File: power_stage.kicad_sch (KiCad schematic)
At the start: 39 parts, among them IC2 L6498D, IC6 L6498D, IC7 L6498D, Q1 IPB320N20N3GATMA1, Q2 IPB320N20N3GATMA1, Q3 IPB320N20N3GATMA1, Q4 IPB320N20N3GATMA1, Q5 IPB320N20N3GATMA1, Q6 IPB320N20N3GATMA1

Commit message: Initial layout
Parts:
- added R24, R33, R34: 2.2Ω, Resistor_SMD:R_0603_1608Metric, symbol Device:R_Small_US
- C17, C18, C2, C20, C3, C8, Cboot1, Cboot2, Cboot3: footprint (none) -> Capacitor_SMD:C_0603_1608Metric
- R1, R10, R12, R13, R14, R15, R2, R3, R4, R7, R8, R9: footprint (none) -> Resistor_SMD:R_0603_1608Metric
- R11, R16, R5: footprint (none) -> Resistor_SMD:R_1206_3216Metric
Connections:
- net +12V: now also R24.2, R33.2, R34.2
- net at IC6.8 (BOOT): now also Cboot2.1, D2.1 (K); no longer D2.2 (A)
- net at Cboot1.1, D1.1 (K): now also IC2.8 (BOOT)
- net at D1.2 (A): now also R24.1; no longer IC2.8 (BOOT)
- net at IC7.8 (BOOT): now also Cboot3.1, D3.1 (K); no longer D3.2 (A)
- new net: D2.2 (A), R33.1
- new net: D3.2 (A), R34.1
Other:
- moved on the sheet: Cboot1, D1

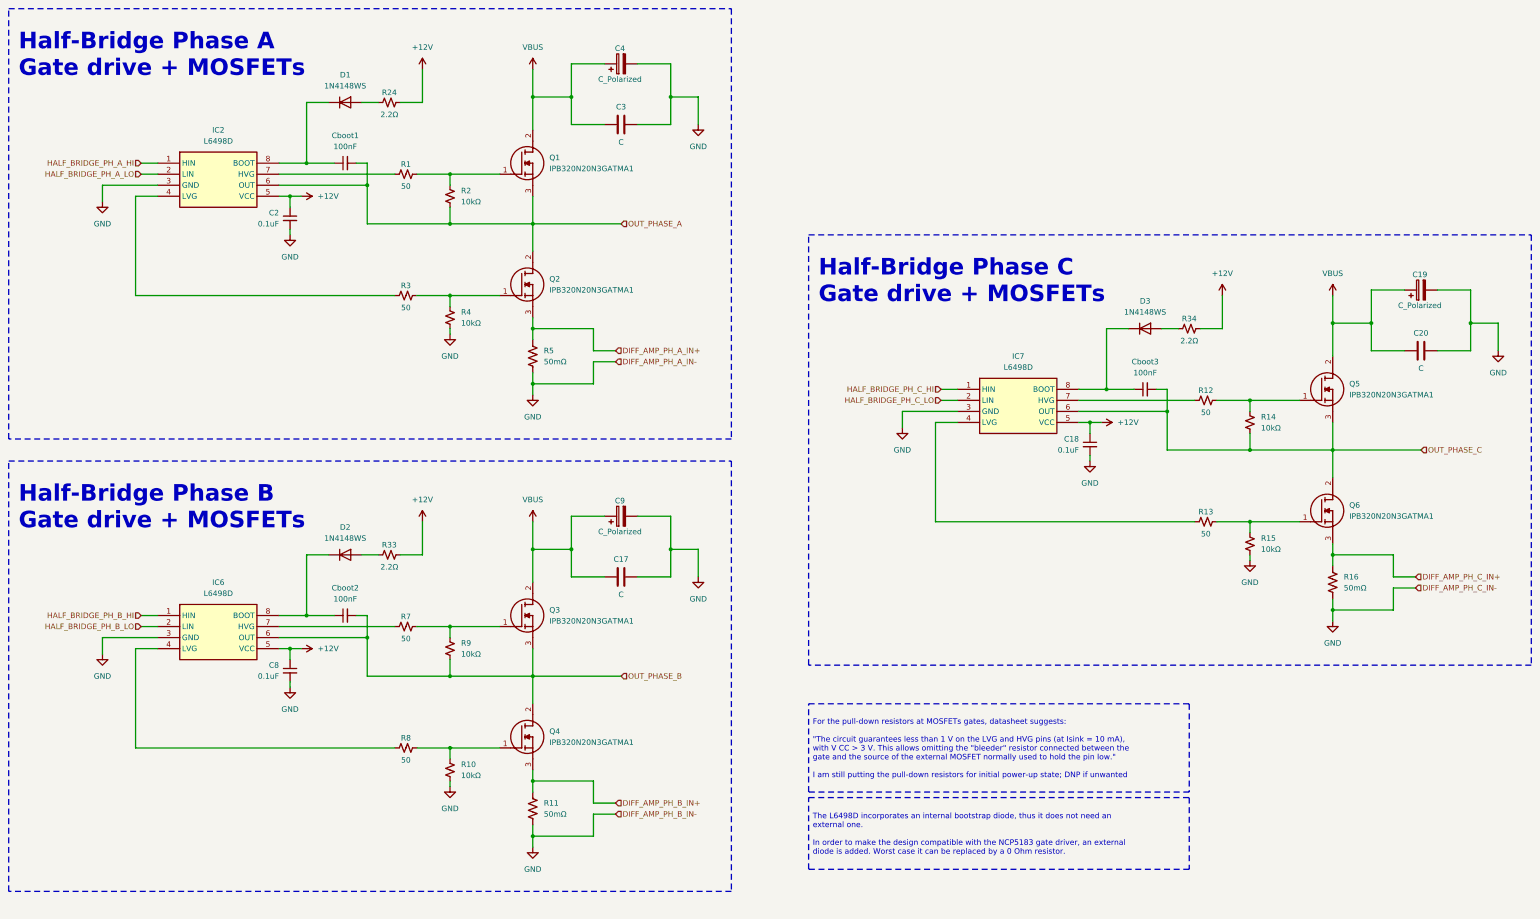
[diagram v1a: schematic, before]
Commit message: Almost all routing done
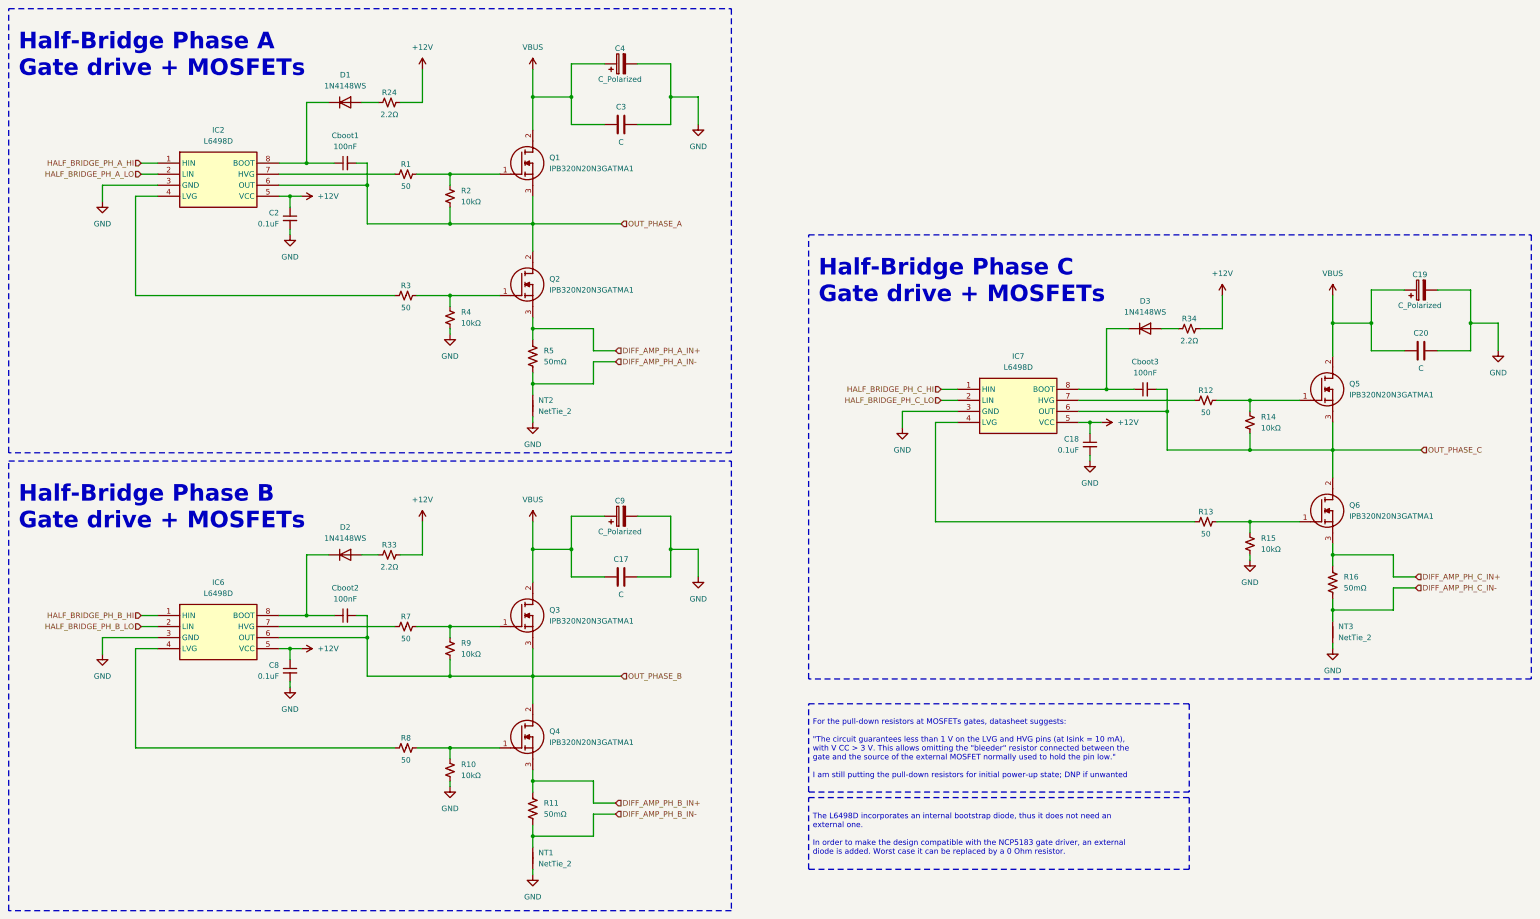
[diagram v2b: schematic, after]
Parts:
- added NT1, NT2, NT3: NetTie_2, NetTie:NetTie-2_SMD_Pad0.5mm, symbol Device:NetTie_2
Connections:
- net GND: now also NT1.1, NT2.1, NT3.1; no longer R11.2, R16.2, R5.2
- new net DIFF_AMP_PH_A_IN-: NT2.2, R5.2
- new net DIFF_AMP_PH_B_IN-: NT1.2, R11.2
- new net DIFF_AMP_PH_C_IN-: NT3.2, R16.2

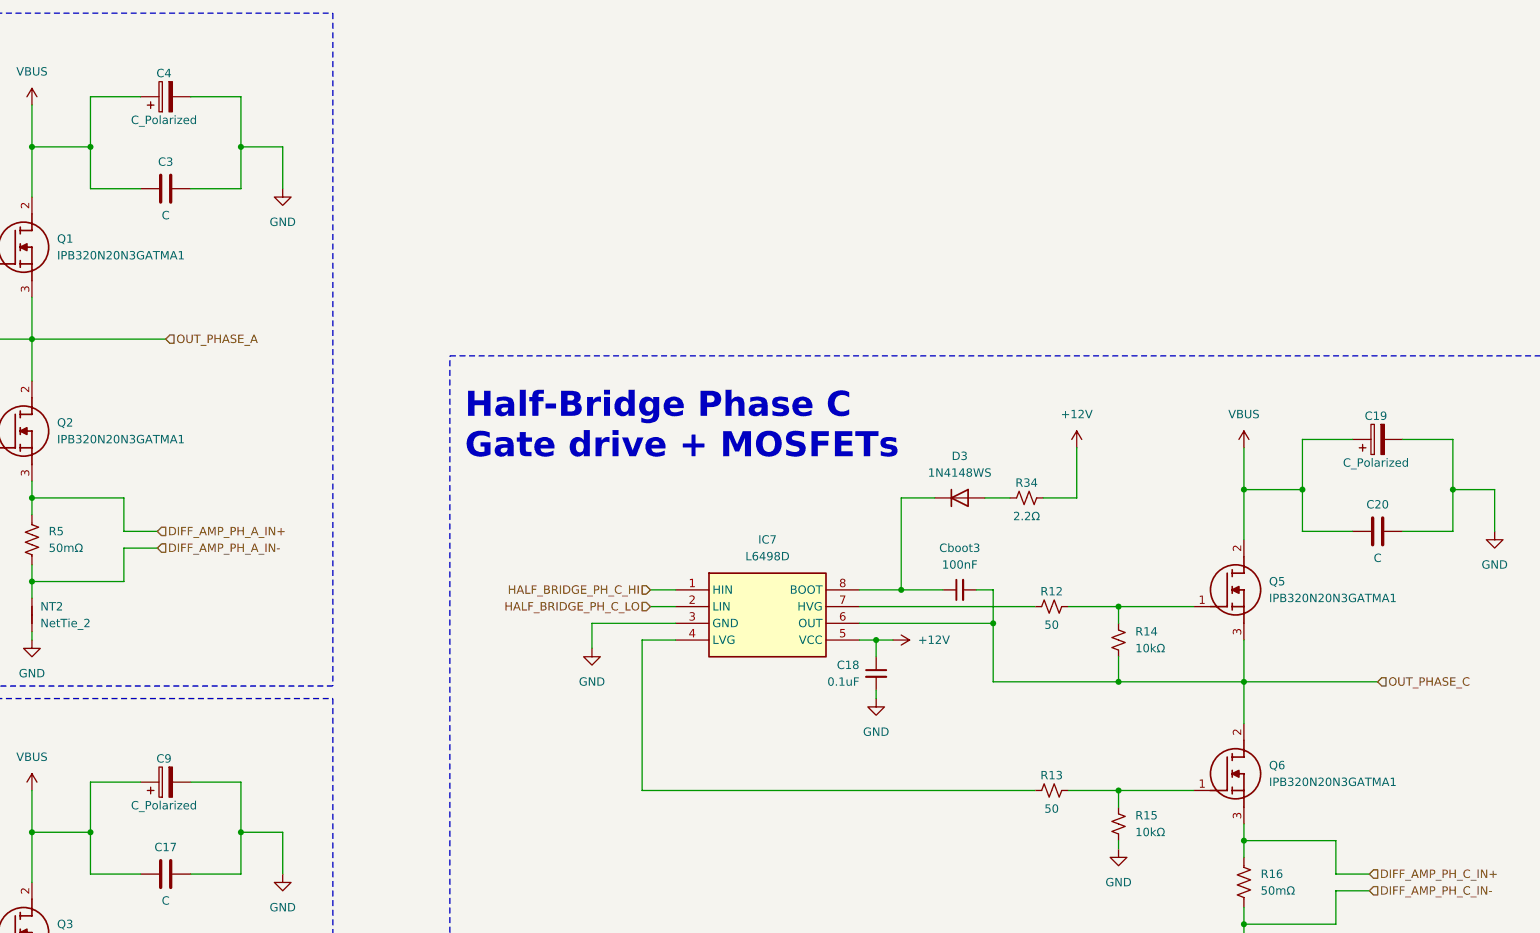
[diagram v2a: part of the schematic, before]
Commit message: Add capacitors
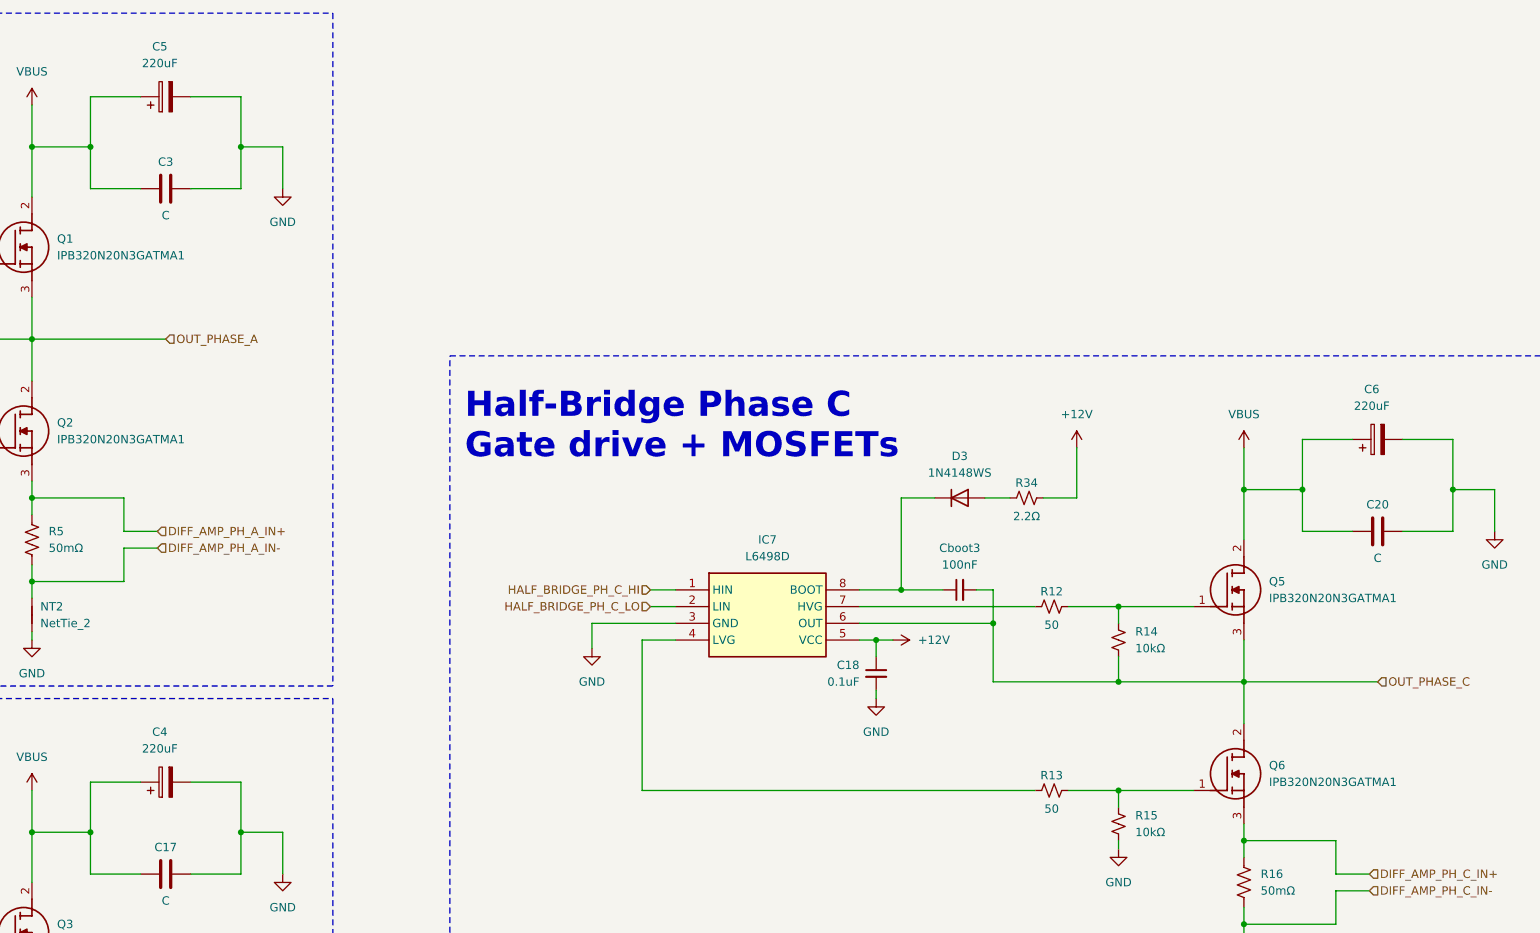
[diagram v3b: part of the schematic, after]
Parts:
- removed C19, C9: C_Polarized, symbol Device:C_Polarized
- added C5, C6: 220uF, BLDC-Motor-Driver:CAPAE1030X1050N, symbol Device:C_Polarized
- C4: value C_Polarized -> 220uF; footprint (none) -> BLDC-Motor-Driver:CAPAE1030X1050N
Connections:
- net GND: now also C5.2, C6.2
- net VBUS: now also C5.1, C6.1

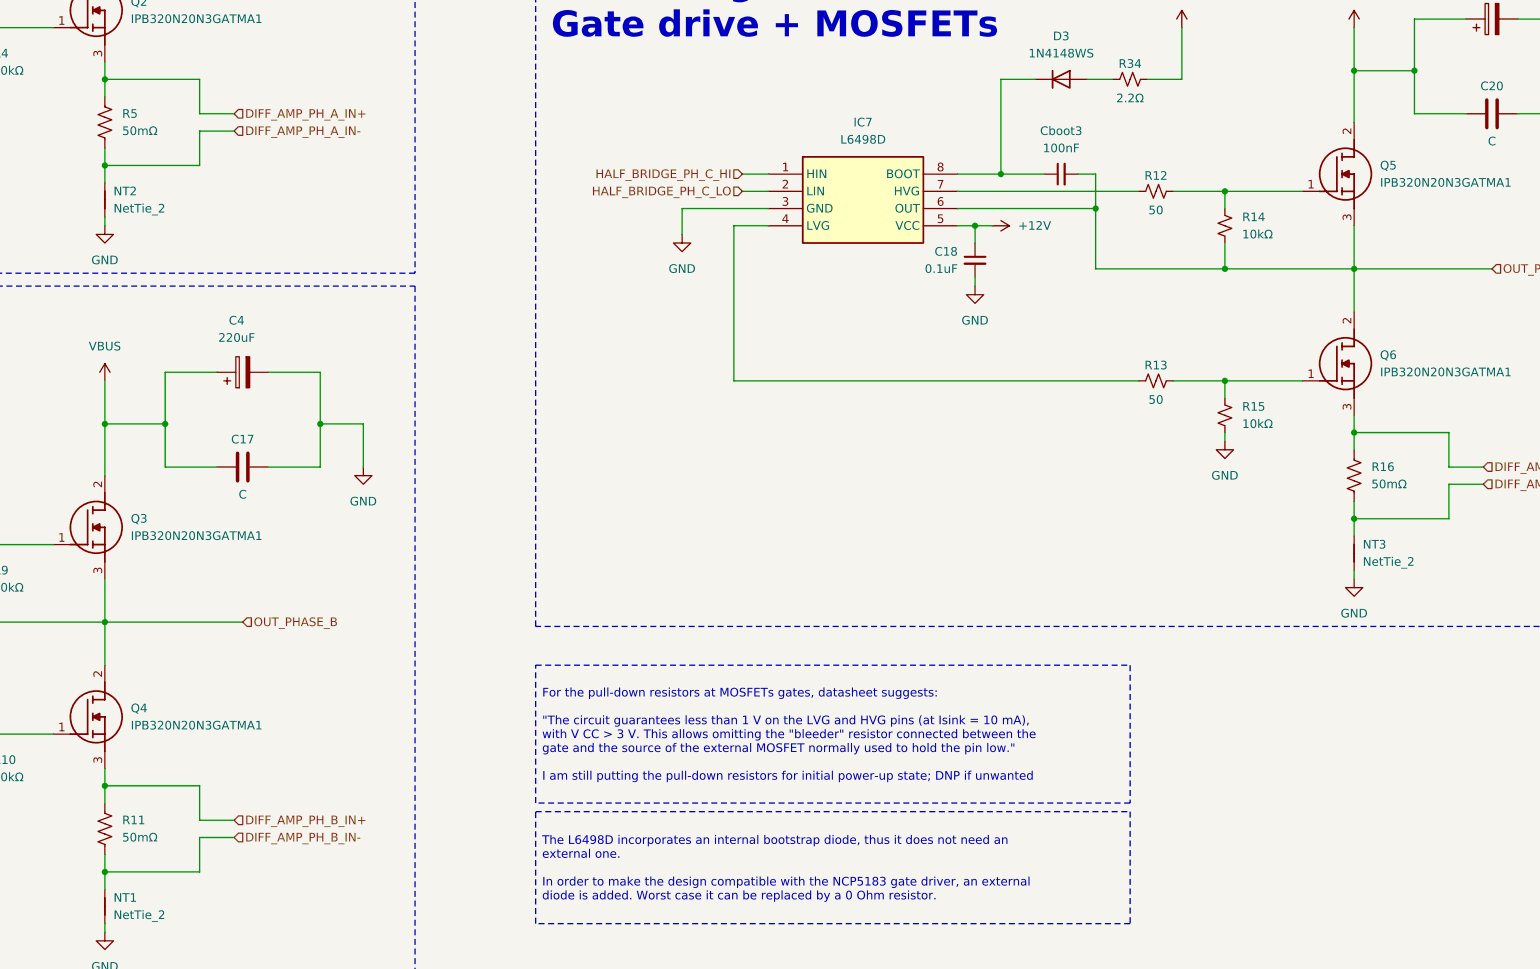
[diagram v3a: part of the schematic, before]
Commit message: Add 5V rail available for LDO input
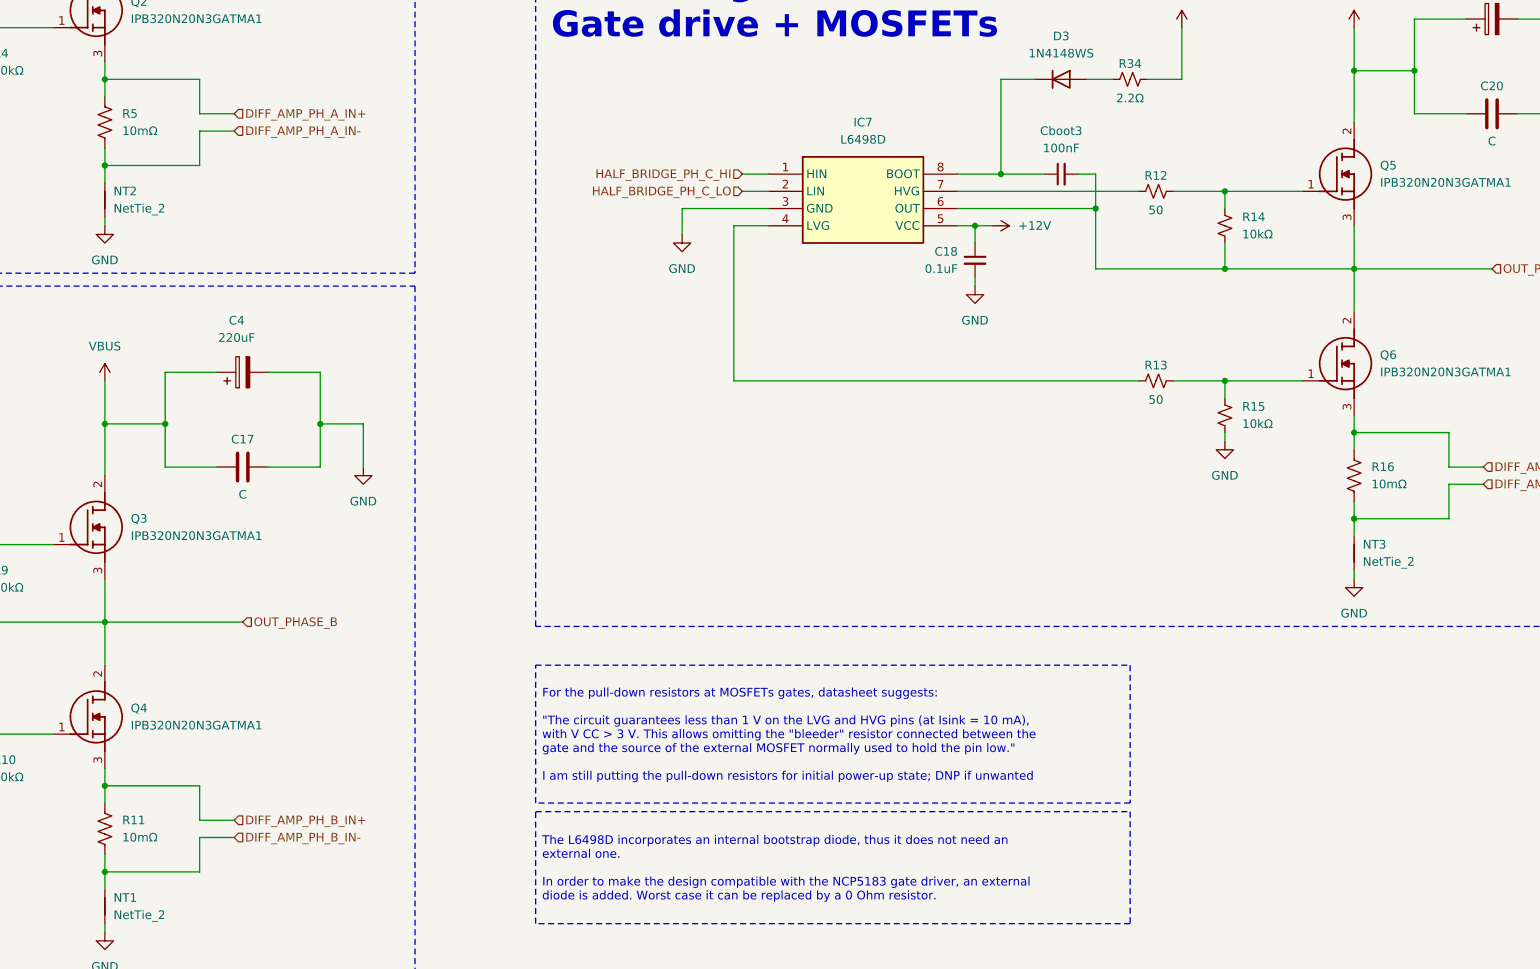
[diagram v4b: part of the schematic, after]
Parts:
- R11, R16, R5: value 50mΩ -> 10mΩ; Manufacturer_Part_Number (none) -> ERJ-L4T12FR010DER
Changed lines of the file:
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@@
 			)
 		)
-		(property "Value" "50mΩ"
+		(property "Value" "10mΩ"
 			(at 344.17 172.7199 0)
 			(effects
@@
 		)
 		(property "Description" "Resistor, US symbol"
+			(at 341.63 171.45 0)
+			(effects
+				(font
+					(size 1.27 1.27)
+				)
+				(hide yes)
+			)
+		)
+		(property "Manufacturer_Part_Number" "ERJ-L4T12FR010DER"
 			(at 341.63 171.45 0)
 			(effects
@@
 	)
 	(symbol
+		(lib_id "Device:R_US")
+		(at 157.48 223.52 0)
+		(unit 1)
+		(exclude_from_sim no)
+		(in_bom yes)
+		(on_board yes)
+		(dnp no)
+		(property "Reference" "R11"
+			(at 160.02 222.2499 0)
+			(effects
+				(font
+					(size 1.27 1.27)
+				)
+				(justify left)
+			)
+		)
+		(property "Value" "10mΩ"
+			(at 160.02 224.7899 0)
+			(effects
+				(font
+					(size 1.27 1.27)
+				)
+				(justify left)
+			)
+		)
+		(property "Footprint" "Resistor_SMD:R_1206_3216Metric"
+			(at 158.496 223.774 90)
+			(effects
+				(font
+					(size 1.27 1.27)
+				)
+				(hide yes)
+			)
+		)
+		(property "Datasheet" "~"
+			(at 157.48 223.52 0)
+			(effects
+				(font
+					(size 1.27 1.27)
+				)
+				(hide yes)
+			)
+		)
+		(property "Description" "Resistor, US symbol"
+			(at 157.48 223.52 0)
+			(effects
+				(font
+					(size 1.27 1.27)
+				)
+				(hide yes)
+			)
+		)
+		(property "Manufacturer_Part_Number" "ERJ-L4T12FR010DER"
+			(at 157.48 223.52 0)
+			(effects
+				(font
+					(size 1.27 1.27)
+				)
+				(hide yes)
+			)
+		)
+		(pin "1"
+		)
+		(pin "2"
+		)
+		(instances
+			(project "BLDC_Motor_Driver"
+				(path "/7abcc48e-1931-446f-8daf-9260c9f942ba/6881e12c-11b3-44bc-8480-7acbf9300e67"
+					(reference "R11")
+					(unit 1)
+				)
+			)
+		)
+	)
+	(symbol
 		(lib_id "power:+12V")
 		(at 104.14 82.55 270)
@@
 			)
 		)
-		(property "Value" "50mΩ"
+		(property "Value" "10mΩ"
 			(at 160.02 120.6499 0)
 			(effects
@@
 		)
 		(property "Description" "Resistor, US symbol"
+			(at 157.48 119.38 0)
+			(effects
+				(font
+					(size 1.27 1.27)
+				)
+				(hide yes)
+			)
+		)
+		(property "Manufacturer_Part_Number" "ERJ-L4T12FR010DER"
 			(at 157.48 119.38 0)
 			(effects
@@
 					(unit 1)
 				)
-			)
-		)
-	)
-	(symbol
-		(lib_id "Device:R_US")
-		(at 157.48 223.52 0)
-		(unit 1)
-		(exclude_from_sim no)
-		(in_bom yes)
-		(on_board yes)
-		(dnp no)
-		(property "Reference" "R11"
-			(at 160.02 222.2499 0)
-			(effects
-				(font
-					(size 1.27 1.27)
-				)
-				(justify left)
-			)
-		)
-		(property "Value" "50mΩ"
-			(at 160.02 224.7899 0)
-			(effects
-				(font
-					(size 1.27 1.27)
-				)
-				(justify left)
-			)
-		)
-		(property "Footprint" "Resistor_SMD:R_1206_3216Metric"
-			(at 158.496 223.774 90)
-			(effects
-				(font
-					(size 1.27 1.27)
-				)
-				(hide yes)
-			)
-		)
-		(property "Datasheet" "~"
-			(at 157.48 223.52 0)
-			(effects
-				(font
-					(size 1.27 1.27)
-				)
-				(hide yes)
-			)
-		)
-		(property "Description" "Resistor, US symbol"
-			(at 157.48 223.52 0)
-			(effects
-				(font
-					(size 1.27 1.27)
-				)
-				(hide yes)
-			)
-		)
-		(pin "1"
-		)
-		(pin "2"
-		)
-		(instances
-			(project "BLDC_Motor_Driver"
-				(path "/7abcc48e-1931-446f-8daf-9260c9f942ba/6881e12c-11b3-44bc-8480-7acbf9300e67"
-					(reference "R11")
-					(unit 1)
-				)
